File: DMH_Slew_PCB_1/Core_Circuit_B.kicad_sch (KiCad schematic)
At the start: 29 parts, among them Q1 BC548, Q2 BC558, Q3 BC558, Q4 BC548, SW1 SW_SPDT, SW2 SW_DPDT, U3 TL074

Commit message: Schematic design in progress
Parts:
- removed SW2: SW_DPDT, SynthStuff:Toggle_Switch_2_Poles_TE, symbol SynthStuff:Switch_DPDT
- SW2: renamed from SW1; Function (none) -> Lin / Exp
- renumbered C6 to C7, C5 to C8, Q1 to Q5, Q2 to Q6, Q3 to Q7, Q4 to Q8, R20 to R28, R21 to R29, R22 to R30, R23 to R31, R16 to R32, R18 to R33, R19 to R34, R17 to R35, R15 to R36, R12 to R37, R13 to R38, R11 to R39, R14 to R40, R5 to R41, R2 to R42, R7 to R43, R9 to R44, R10 to R45, R6 to R46, R8 to R47, U3 to U4
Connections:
- net B Fall Pot: now reaches R31.2
- net B Fall CV: now reaches R30.2
- net Input A renamed Input B
- net Output A renamed Output B
- net Slew A CV renamed B Rise CV
- net Slew A Pot G1 renamed B Rise Pot

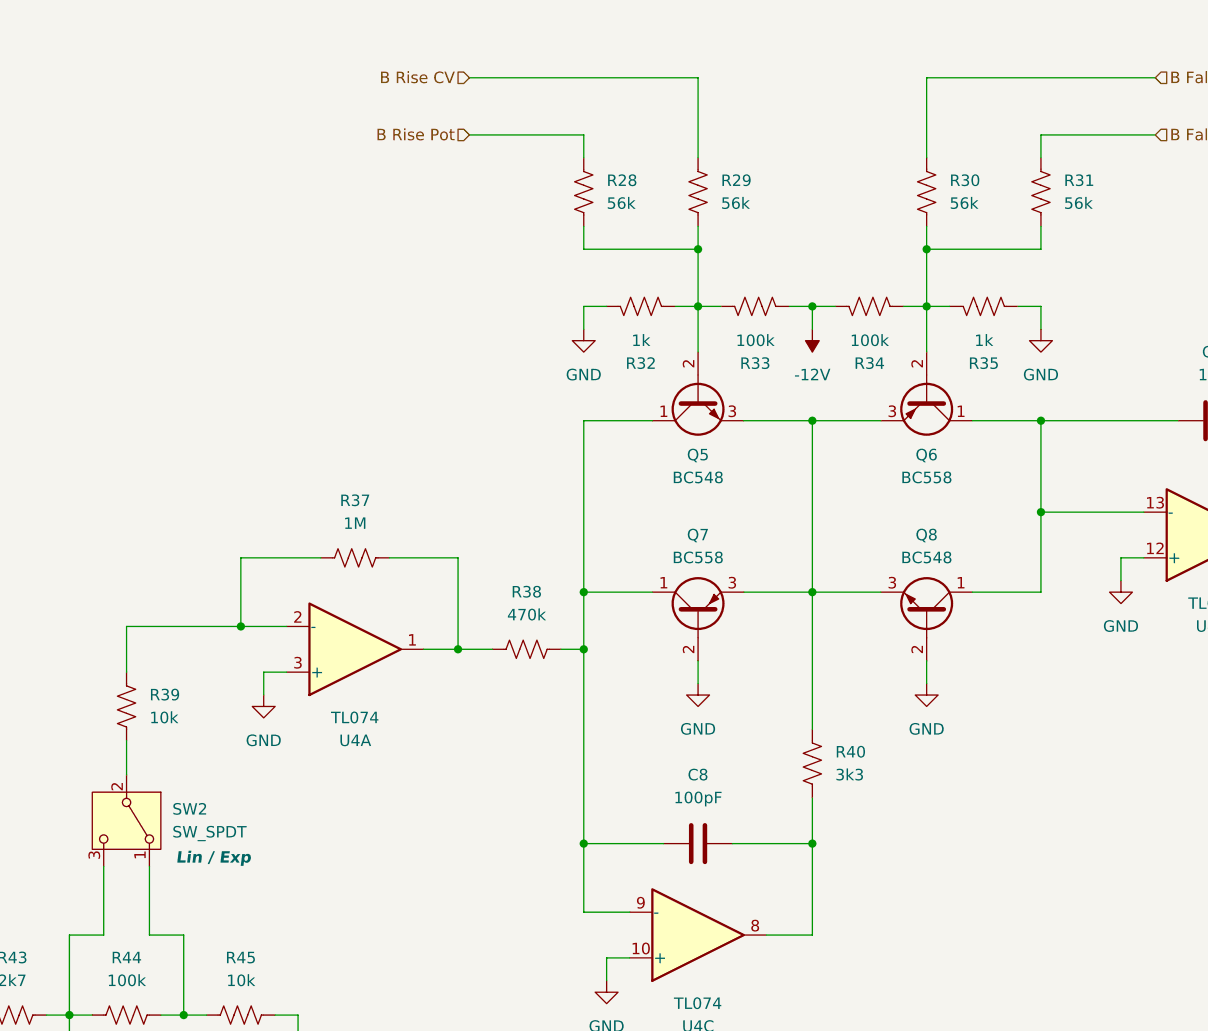
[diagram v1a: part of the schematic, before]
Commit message: Applied 10V to pots
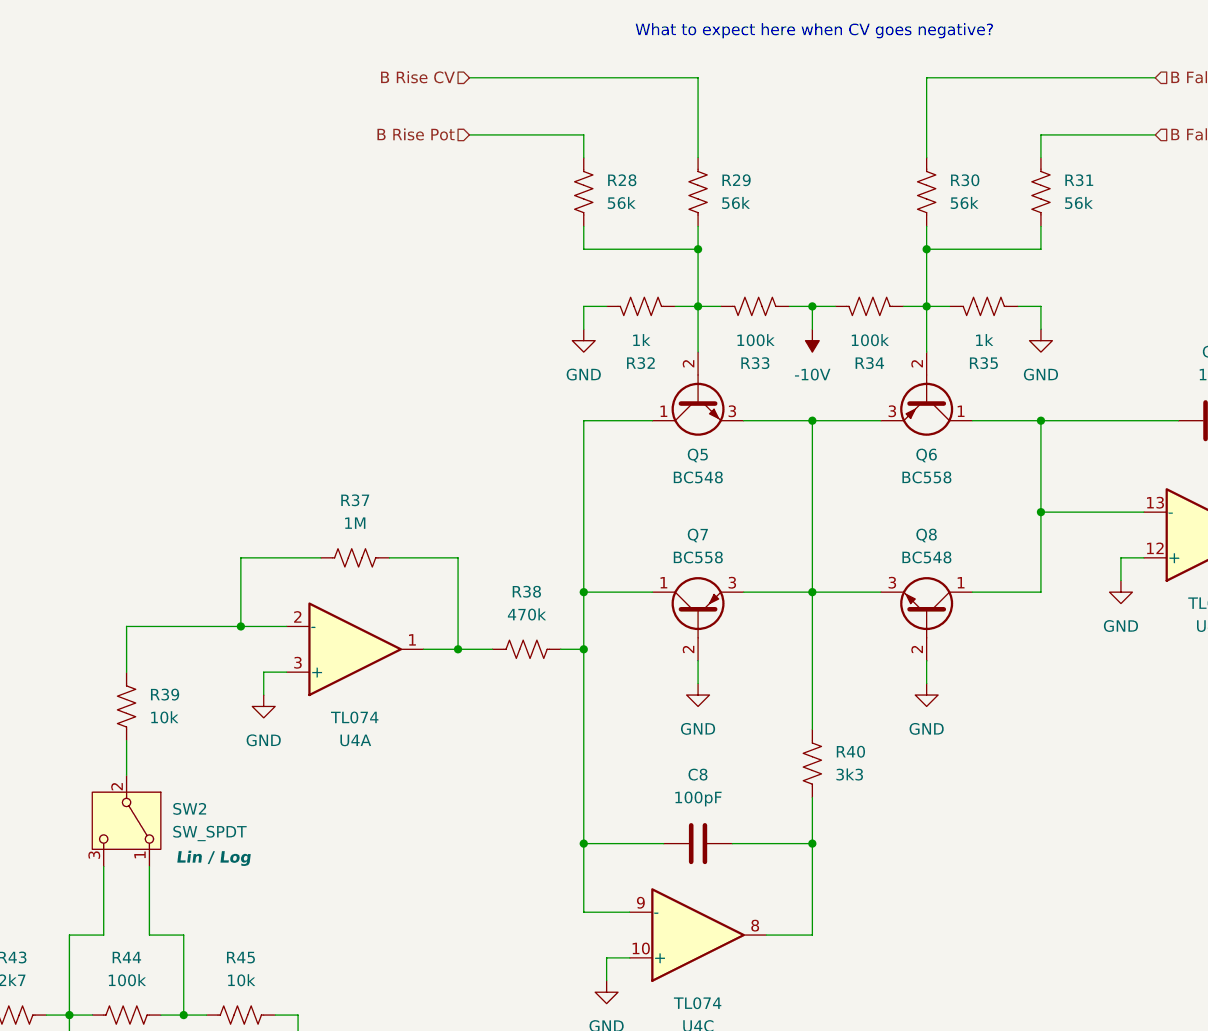
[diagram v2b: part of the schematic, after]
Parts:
- SW2: Function Lin / Exp -> Lin / Log
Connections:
- net -12V renamed -10V
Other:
- note added: "What to expect here when CV goes negative?"
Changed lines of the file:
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@@
 		(comment 1 "PCB for 5 cm Kosmo format synthesizer module")
+	)
+	(text "What to expect here when CV goes negative?"
+		(exclude_from_sim no)
+		(at 165.354 33.02 0)
+		(effects
+			(font
+				(size 1.27 1.27)
+			)
+		)
 	)
 	(junction
@@
 	)
 	(symbol
-		(lib_id "power:-12V")
+		(lib_id "power:-10V")
 		(at 165.1 66.04 180)
 		(unit 1)
@@
 			)
 		)
-		(property "Value" "-12V"
+		(property "Value" "-10V"
 			(at 165.1 71.12 0)
 			(effects
@@
 			)
 		)
-		(property "Description" "Power symbol creates a global label with name \"-12V\""
+		(property "Description" "Power symbol creates a global label with name \"-10V\""
 			(at 165.1 66.04 0)
 			(effects
@@
 			)
 		)
-		(property "Function" "Lin / Exp"
+		(property "Function" "Lin / Log"
 			(at 98.552 124.714 90)
 			(effects

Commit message: Exported preliminary BoM
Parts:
- SW2: footprint (none) -> SynthStuff:Toggle_Switch_TE
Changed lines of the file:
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@@
 			)
 		)
-		(property "Footprint" ""
+		(property "Footprint" "SynthStuff:Toggle_Switch_TE"
 			(at 88.9 120.65 0)
 			(effects

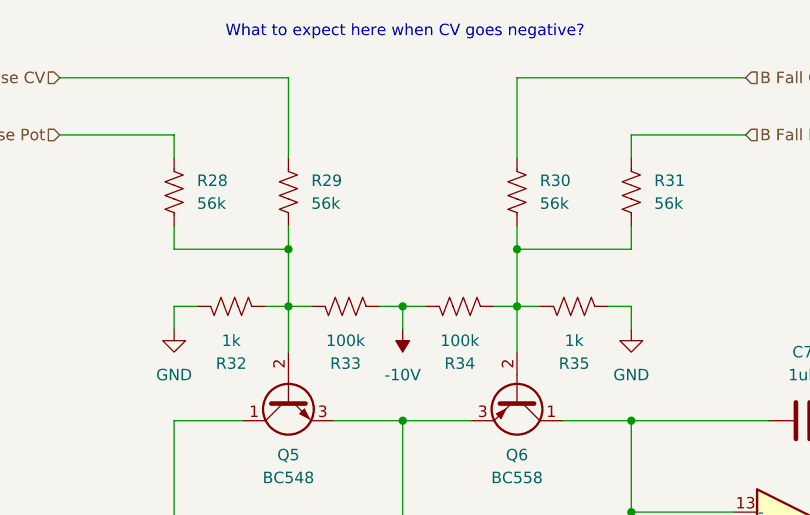
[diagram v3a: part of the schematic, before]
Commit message: Simulated core circuit
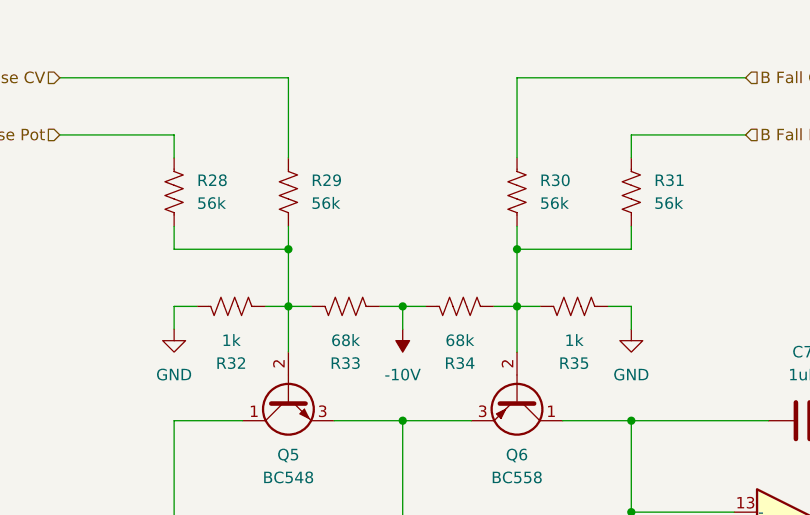
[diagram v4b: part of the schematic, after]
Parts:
- R33, R34: value 100k -> 68k
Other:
- note removed: "What to expect here when CV goes negative?"
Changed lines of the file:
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@@
 		(comment 1 "PCB for 5 cm Kosmo format synthesizer module")
-	)
-	(text "What to expect here when CV goes negative?"
-		(exclude_from_sim no)
-		(at 165.354 33.02 0)
-		(effects
-			(font
-				(size 1.27 1.27)
-			)
-		)
 	)
 	(junction
@@
 			)
 		)
-		(property "Value" "100k"
+		(property "Value" "68k"
 			(at 158.75 67.31 90)
 			(effects
@@
 				)
 				(hide yes)
+			)
+		)
+		(property "Function" ""
+			(at 158.75 63.5 0)
+			(effects
+				(font
+					(size 1.27 1.27)
+				)
 			)
 		)
@@
 			)
 		)
-		(property "Value" "100k"
+		(property "Value" "68k"
 			(at 171.45 67.31 90)
 			(effects
@@
 			)
 		)
+		(property "Function" ""
+			(at 171.45 63.5 0)
+			(effects
+				(font
+					(size 1.27 1.27)
+				)
+			)
+		)
